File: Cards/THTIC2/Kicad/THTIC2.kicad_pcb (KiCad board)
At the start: 2 copper layers, 50.3 x 24.1 mm, 25 parts, among them J1 Conn_01x04_Pin, J2 Plasma 300V, U1 B0509S-1WR3, U2 ISO1540, U3 ADS1014IDGS, U4 AMS1117-5, U5 LMV321

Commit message: SCL instead of SDL
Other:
- board text added: "5V SDA SCL GND"
- board text removed: "5V SDA SDL GND"
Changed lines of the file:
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@@
 		)
 	)
-	(gr_text "5V\n\nSDA\n\nSDL\n\nGND"
+	(gr_text "5V\n\nSDA\n\nSCL\n\nGND"
 		(at 191.262 105.029 0)
 		(layer "B.SilkS")

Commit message: Final version of THTIC2
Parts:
- added H4: MountingHole, MountingHole:MountingHole_3.2mm_M3, F.Cu at (155.2, 104.8)
- added R8: 2k2, Resistor_SMD:R_0805_2012Metric, F.Cu at (190.0, 96.9)
- R4: value nP -> 2k2
- R6: value 1k27 -> 2k1
- moved R4 25.0 mm to (191.9, 96.9), turned to 90 degrees
- moved H2 9.55 mm to (188.8, 104.8)
- moved D1 9.33 mm to (170.3, 102.6)
- moved R5 7.21 mm to (168.0, 96.0), turned to 180 degrees
- moved H1 5.20 mm to (188.8, 88.4)
- moved R6 4.92 mm to (163.4, 96.0), turned to 0 degrees
- moved J1 4.41 mm to (196.3, 90.5)
- moved U1 4.25 mm to (182.7, 87.1)
- moved R7 3.97 mm to (162.3, 101.3)
- moved C5 3.64 mm to (171.6, 96.0)
- moved C7 3.40 mm to (167.1, 102.4)
- moved J2 3.39 mm to (156.6, 98.4)
- moved C6 3.21 mm to (161.9, 92.6)
- moved C3 2.99 mm to (171.5, 92.3)
- moved U4 2.99 mm to (166.8, 90.3)
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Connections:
- C7 pad 1: Net-(D2-COM) -> Net-(D1-COM)
- D1 pad 3: Net-(D2-COM) -> Net-(D1-COM)
- R3 pad 2: Net-(U7--) -> Net-(U5--)
- R4 pad 1: Net-(U7--) -> 5V
- R4 pad 2: Net-(D2-COM) -> Net-(J1-Pin_2)
- R5 pad 1: Net-(D2-COM) -> Net-(D1-COM)
- U5 pad 1: Net-(D2-COM) -> Net-(D1-COM)
- U5 pad 3: Net-(U7--) -> Net-(U5--)
- U5 pad 4: Net-(U7--) -> Net-(U5--)
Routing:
- net GND: track 10.7 -> 35.7 mm, vias 29 -> 34
- net GND_ISO: track 105.5 -> 124.2 mm, vias 76 -> 56
- net Net-(D2-COM): track 17.6 -> 0.00 mm
- net Net-(D1-COM): track 0.00 -> 10.4 mm
- net Net-(U7--): track 10.1 -> 0.00 mm
- net Net-(U5--): track 0.00 -> 5.16 mm
- net Net-(U2-SDA2): track 8.37 -> 13.2 mm
- net Net-(J1-Pin_2): track 8.09 -> 12.5 mm
- net 5V: track 37.6 -> 41.5 mm
- net Net-(J1-Pin_3): track 16.7 -> 20.3 mm
- net Net-(U2-SCL2): track 11.1 -> 8.04 mm
- net Net-(U3-AIN0): track 4.30 -> 2.10 mm
- net VCC_ISO: track 46.1 -> 44.9 mm
- net Net-(J2-Pin_1): track 7.19 -> 8.31 mm
- net Net-(U1-+Vout): track 9.98 -> 9.07 mm
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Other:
- board size 50.3 x 24.1 mm -> 50.9 x 24.5 mm
- board text added: "MetalMusings THTIC2 Feb 2025"
- board text removed: "MetalMusings THTIC2 prototype 1 Feb 2025"

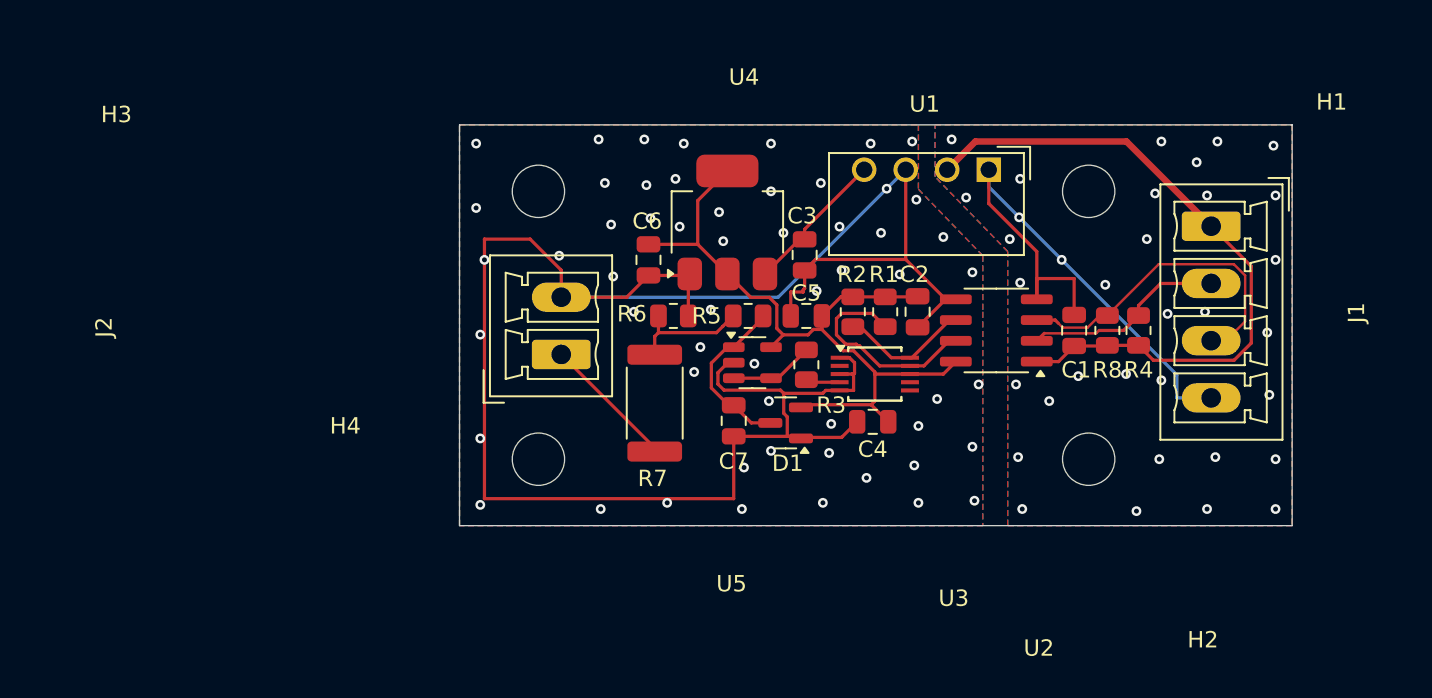
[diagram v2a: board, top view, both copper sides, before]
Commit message: Now measuring 0 - -200 Volts.
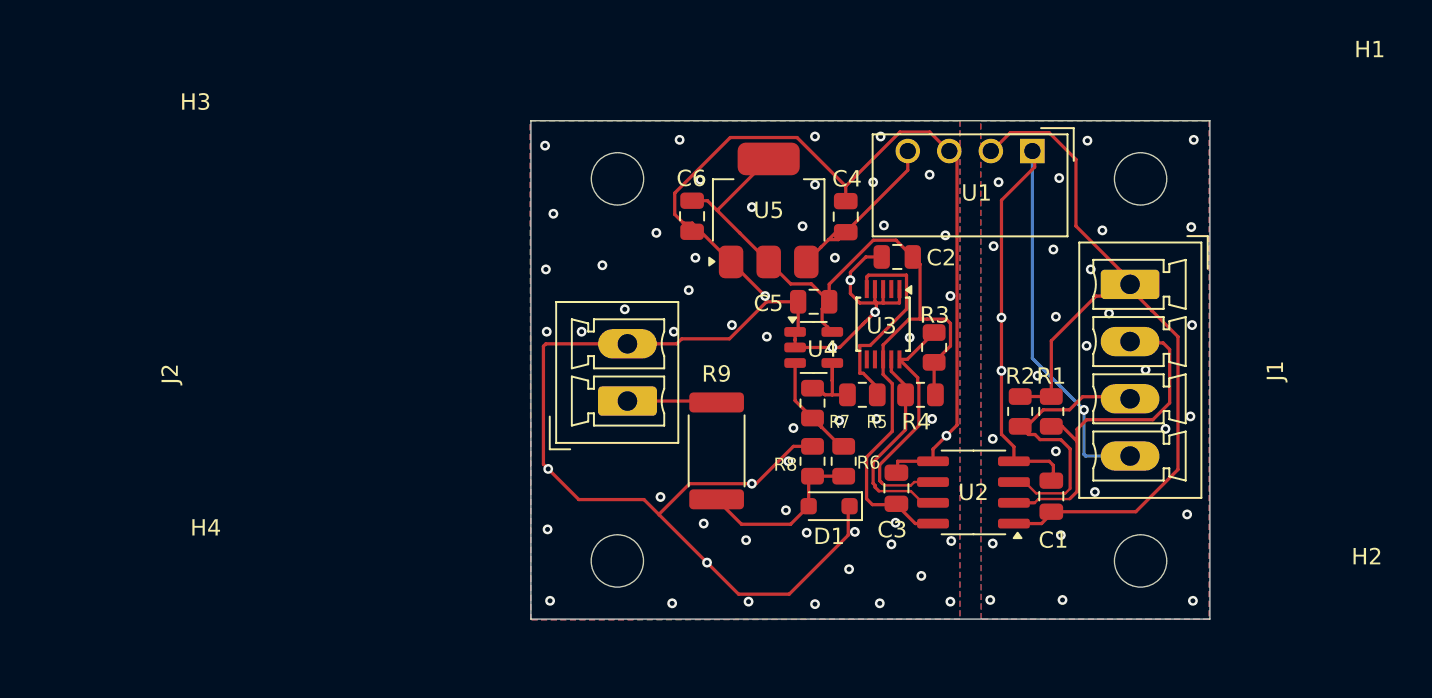
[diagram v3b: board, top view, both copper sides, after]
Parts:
- removed the C5 at (171.6, 96.0)
- removed C7: 1nF, Capacitor_SMD:C_0805_2012Metric
- removed the H4 at (155.2, 104.8)
- removed the R8 at (190.0, 96.9)
- added C2: 100nF, Capacitor_SMD:C_0805_2012Metric, F.Cu at (177.1, 92.4)
- added H2: MountingHole, MountingHole:MountingHole_3.2mm_M3, F.Cu at (192.0, 111.0)
- added R2: 2k2, Resistor_SMD:R_0805_2012Metric, F.Cu at (184.7, 101.9)
- added R7: 100k, Resistor_SMD:R_0805_2012Metric, F.Cu at (172.0, 101.3)
- C6: value 22uF Tant -> 10uF
- D1: value BAT54S -> 5.1V Zener; footprint Package_TO_SOT_SMD:SOT-23 -> Diode_SMD:D_SOD-323_HandSoldering
- J2: value Plasma 300V -> Plasma 200V
- R6: renamed from R5; value 10k -> 100k
- R8: renamed from R6; value 2k1 -> 2k7
- moved H4 29.5 mm to (160.0, 111.0)
- moved R8 12.3 mm to (172.0, 104.9), turned to 90 degrees
- moved C3 10.9 mm to (177.1, 106.6), turned to 90 degrees
- moved R6 10.6 mm to (173.9, 104.9), turned to -90 degrees
- moved C1 10.2 mm to (186.6, 107.0)
- moved U2 10.0 mm to (181.8, 106.8)
- moved C5 8.18 mm to (172.0, 95.1)
- moved R1 7.28 mm to (186.6, 101.9), turned to -90 degrees
- moved J1 6.10 mm to (191.4, 94.1)
- moved D1 5.75 mm to (173.0, 107.6)
- moved R4 5.52 mm to (178.6, 100.8), turned to 180 degrees
- moved R3 5.43 mm to (179.4, 97.9), turned to 90 degrees
- moved J2 4.95 mm to (160.6, 101.2)
- moved H3 4.90 mm to (160.0, 87.6)
- moved R9 4.78 mm to (166.1, 104.3), turned to -90 degrees
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- renumbered C2 to C3, C3 to C4, C4 to C5, H2 to H4, R4 to R1, R2 to R3, R1 to R4, R3 to R5, R7 to R9, U5 to U4, U4 to U5
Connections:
- D1 pad 2: VCC_ISO -> Net-(D1-A)
- R5 pad 1: Net-(U3-AIN0) -> Net-(U3-AIN1)
- R5 pad 2: Net-(U5--) -> Net-(R5-Pad2)
- R6 pad 1: Net-(D1-COM) -> Net-(U4--)
- R6 pad 2: Net-(R5-Pad2) -> Net-(D1-A)
- R8 pad 1: Net-(R5-Pad2) -> Net-(D1-A)
- R9 pad 2: Net-(R5-Pad2) -> Net-(D1-A)
- U3 pad 4: Net-(U3-AIN0) -> GND_ISO
- U3 pad 5: GND_ISO -> Net-(U3-AIN1)
- U4 pad 1: Net-(D1-COM) -> GND_ISO
- U4 pad 3: Net-(U5--) -> Net-(U4--)
- U4 pad 4: Net-(U5--) -> Net-(R5-Pad2)
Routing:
- net Net-(U3-AIN1): track 0.00 -> 12.7 mm
- net GND: track 35.7 -> 46.5 mm, vias 34 -> 29
- net Net-(D1-COM): track 10.4 -> 0.00 mm
- net Net-(D1-A): track 0.00 -> 10.2 mm
- net VCC_ISO: track 44.9 -> 54.2 mm
- net Net-(J1-Pin_2): track 12.5 -> 21.8 mm
- net GND_ISO: track 124.2 -> 132.4 mm, vias 56 -> 58
- net 5V: track 41.5 -> 49.4 mm
- net Net-(U2-SCL2): track 8.04 -> 15.2 mm
- net Net-(U4--): track 0.00 -> 6.65 mm
- net Net-(U5--): track 5.16 -> 0.00 mm
- net Net-(J1-Pin_3): track 20.3 -> 16.0 mm
- net Net-(J2-Pin_1): track 8.31 -> 5.37 mm
- net Net-(R5-Pad2): track 7.46 -> 4.76 mm
- net Net-(U3-AIN0): track 2.10 -> 0.00 mm
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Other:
- board size 50.9 x 24.5 mm -> 41.5 x 30.5 mm
- board text added: "+ Varc - Varc"
- board text added: "MetalMusings THTIC March 2025"
- board text removed: "- Varc + Varc"
- board text removed: "MetalMusings THTIC2 Feb 2025"
